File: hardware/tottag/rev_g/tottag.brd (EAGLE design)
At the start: 68.1 x 39.6 mm, 200 parts, among them J1 USB4110-GF-A, J2 DM3AT-SF-PEJM5, J3 TC2030-JLINK-NL-2SIDE, J4 TC2030-JLINK-NL-2SIDE, J5 MOLEX-PICO-SPOX-3SIDE, Q1 CSD75207W15, Q4 CSD75207W15, T1 HHM1595A1, U1 DW1000, U10 STM32F091CC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

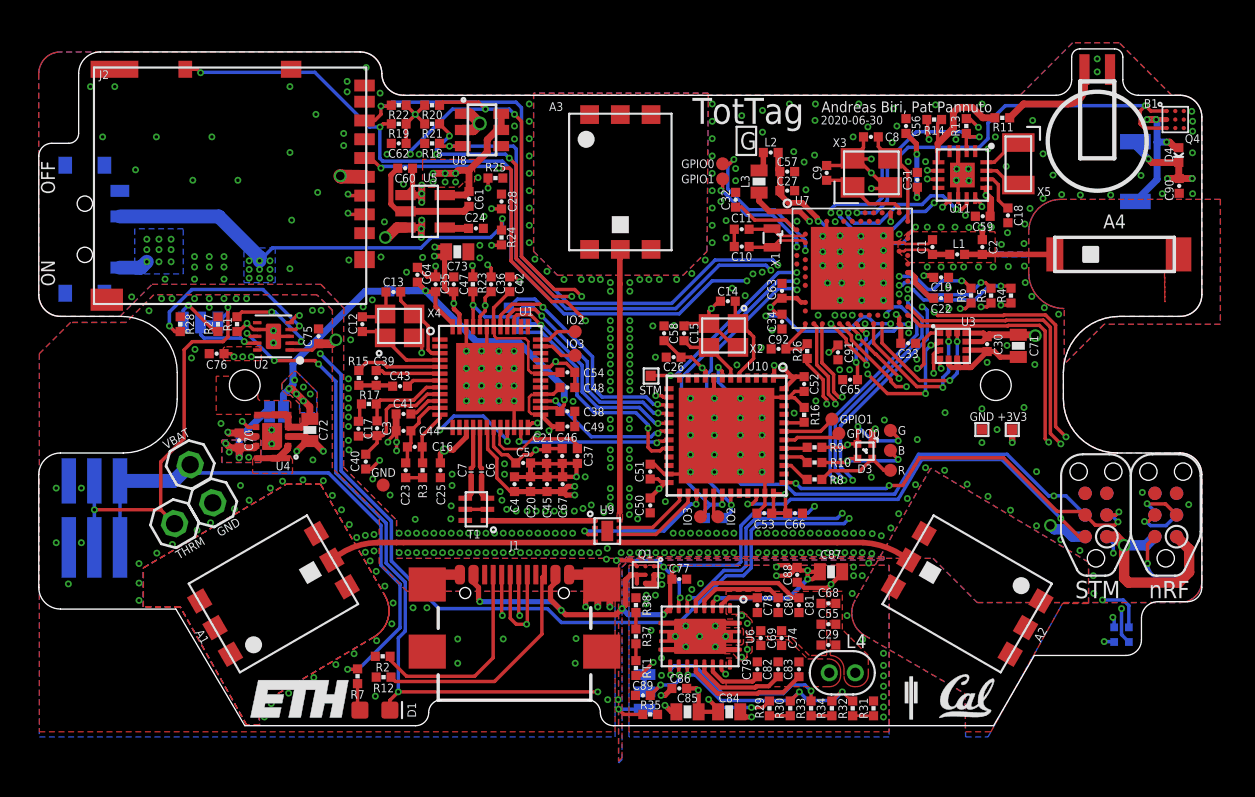
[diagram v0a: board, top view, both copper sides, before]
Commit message: rev_g: [WIP] design review
 - Change !SD_DETECT pin to eliminate major plane cut
 - Clean up ground planes around nrf
 - Move decaps closer to nrf
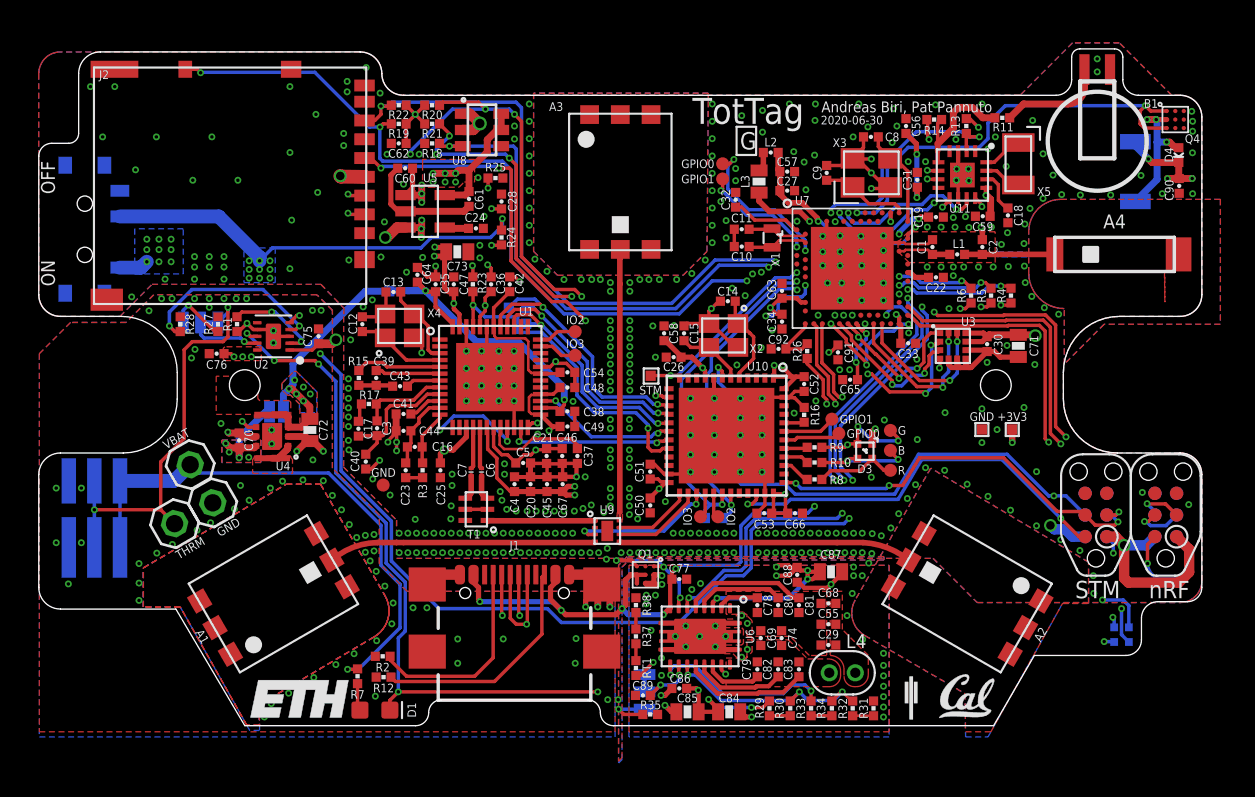
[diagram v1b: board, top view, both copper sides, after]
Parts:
- moved C19 3.54 mm to (18.5, 23.3)
- moved C22 1.26 mm to (18.5, 19.8)
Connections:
- net !SD_DETECT: now also U7.T2; no longer U7.AD22
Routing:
- net !SD_DETECT: track 55.4 -> 50.8 mm
- net NRF_DECAP3: track 3.65 -> 2.19 mm
- net NRF_MISO: track 69.0 -> 68.0 mm
- net NRF_DECAP5: track 2.32 -> 1.34 mm
- net GND: vias 545 -> 546

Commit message: rev_g: rework ground planes and power plane
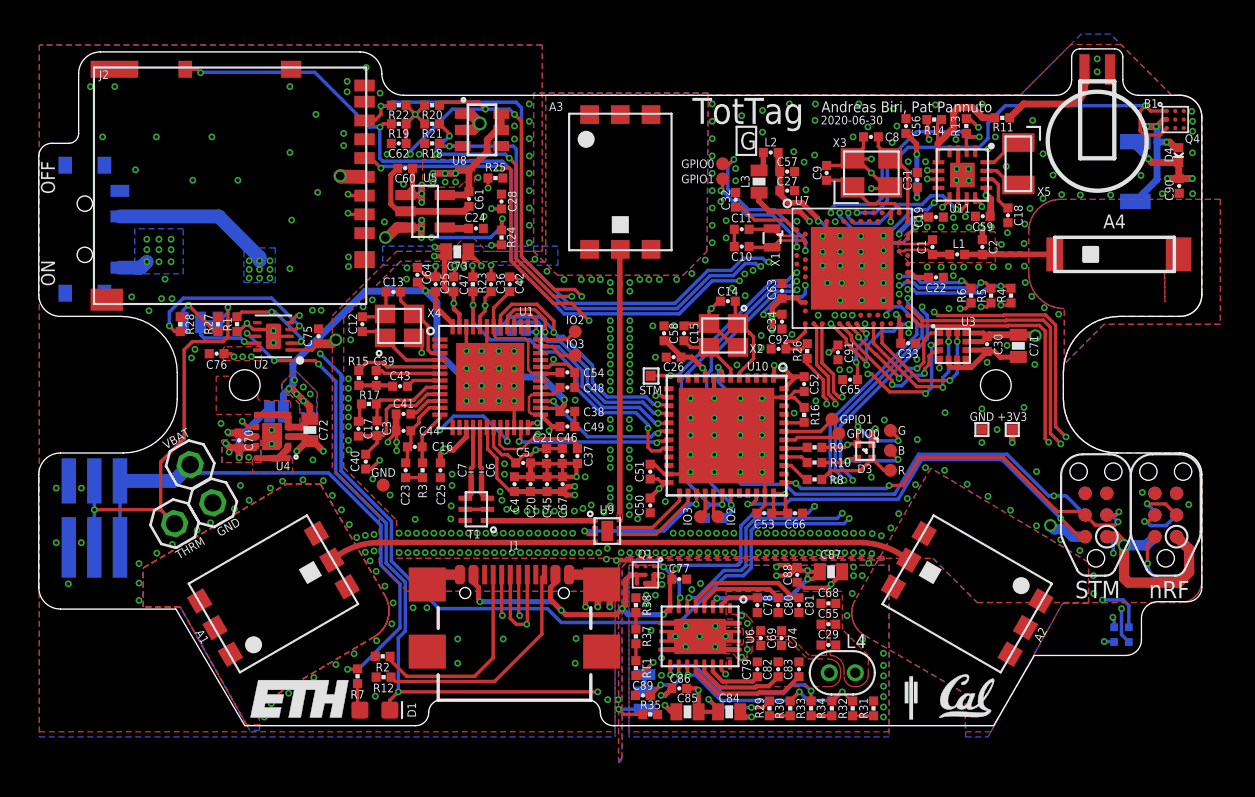
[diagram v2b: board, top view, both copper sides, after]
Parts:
- moved MISO 1.59 mm to (-6.35, 16.7)
- moved SPI_CLK 1.49 mm to (-7.16, 16.7)
- moved MOSI 0.41 mm to (-5.54, 16.7)
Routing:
- net BATIN: track 32.9 -> 30.6 mm
- net DW_SPI_MISO: track 14.8 -> 16.5 mm
- net DW_SPI_CLK: track 16.7 -> 18.3 mm
- net +3V3: track 139.8 -> 140.8 mm, vias 41 -> 42
- net +1V8: track 37.8 -> 37.0 mm
- net BUZZER_GATE: track 25.4 -> 26.0 mm
- net GND: track 168.0 -> 168.2 mm, vias 546 -> 534
- net VBAT: vias 14 -> 15

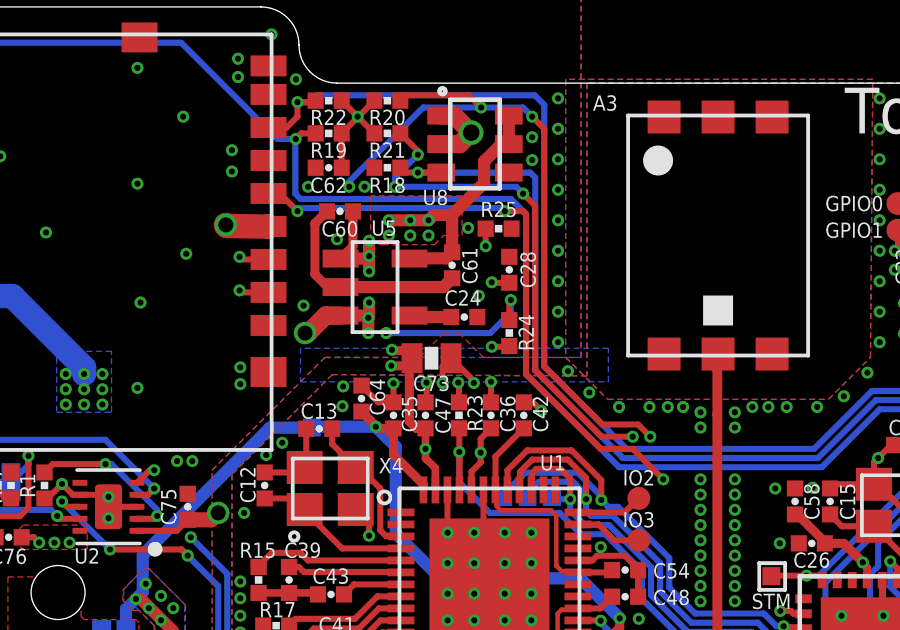
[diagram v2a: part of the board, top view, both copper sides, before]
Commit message: rev_g: change signal for better gnd plane
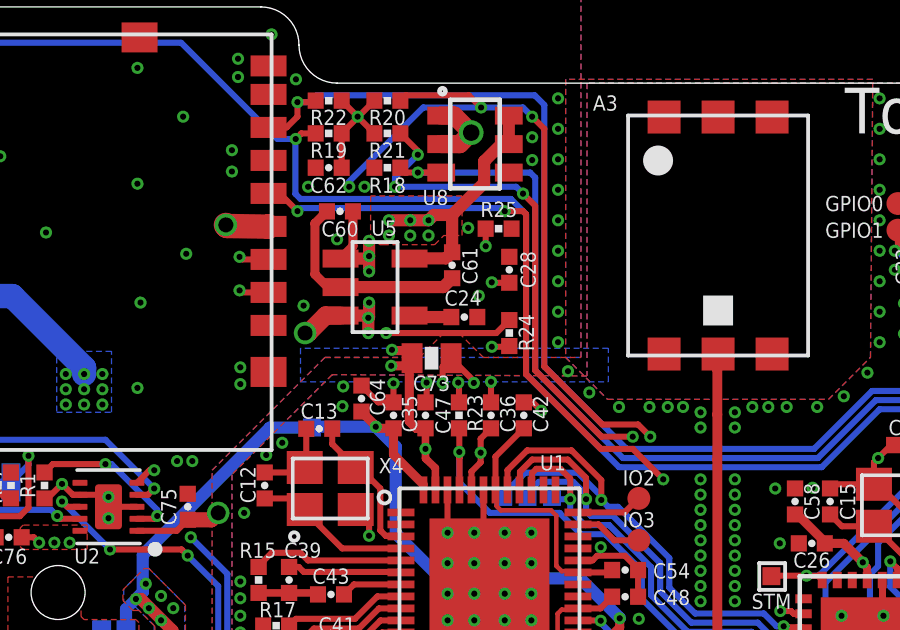
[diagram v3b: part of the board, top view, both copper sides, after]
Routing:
- net VBAT: track 73.1 -> 71.8 mm, vias 15 -> 14
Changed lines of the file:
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@@
 <wire x1="-14.0208" y1="5.2832" x2="-17.0942" y2="8.3566" width="0.2032" layer="16"/>
 <wire x1="-15.3416" y1="-3.1496" x2="-12.9032" y2="-0.7112" width="0.2032" layer="16"/>
-<wire x1="-11.0649375" y1="22.1488" x2="-7.59586875" y2="22.1488" width="0.2032" layer="16"/>
 <contactref element="C76" pad="1"/>
-<wire x1="-6.9088" y1="22.83586875" x2="-6.9088" y2="23.2511625" width="0.2032" layer="16"/>
-<via x="-6.9088" y="23.2511625" extent="1-16" drill="0.2032"/>
-<wire x1="-7.59586875" y1="22.1488" x2="-6.9088" y2="22.83586875" width="0.2032" layer="16"/>
 <contactref element="J6" pad="1"/>
 <wire x1="-25.0444" y1="8.9916" x2="-25.1968" y2="8.8392" width="0.8128" layer="15"/>
@@
 <wire x1="-17.0942" y1="8.3566" x2="-24.7142" y2="8.3566" width="0.2032" layer="16"/>
 <contactref element="R24" pad="2"/>
-<wire x1="-6.9596" y1="22.58186875" x2="-6.9596" y2="23.2003625" width="0.2032" layer="1"/>
-<wire x1="-6.9596" y1="23.2003625" x2="-6.9088" y2="23.2511625" width="0.2032" layer="1"/>
 <polygon width="0.0508" layer="1" thermals="no">
 <vertex x="-21.0312" y="15.748"/>
@@
 </polygon>
 <via x="-11.0649375" y="22.1488" extent="1-16" drill="0.2032"/>
+<wire x1="-11.0649375" y1="22.1488" x2="-7.39266875" y2="22.1488" width="0.2032" layer="1"/>
+<wire x1="-7.39266875" y1="22.1488" x2="-6.9596" y2="22.58186875" width="0.2032" layer="1"/>
 </signal>
 <signal name="BATIN">
